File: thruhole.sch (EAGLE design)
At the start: 10 parts

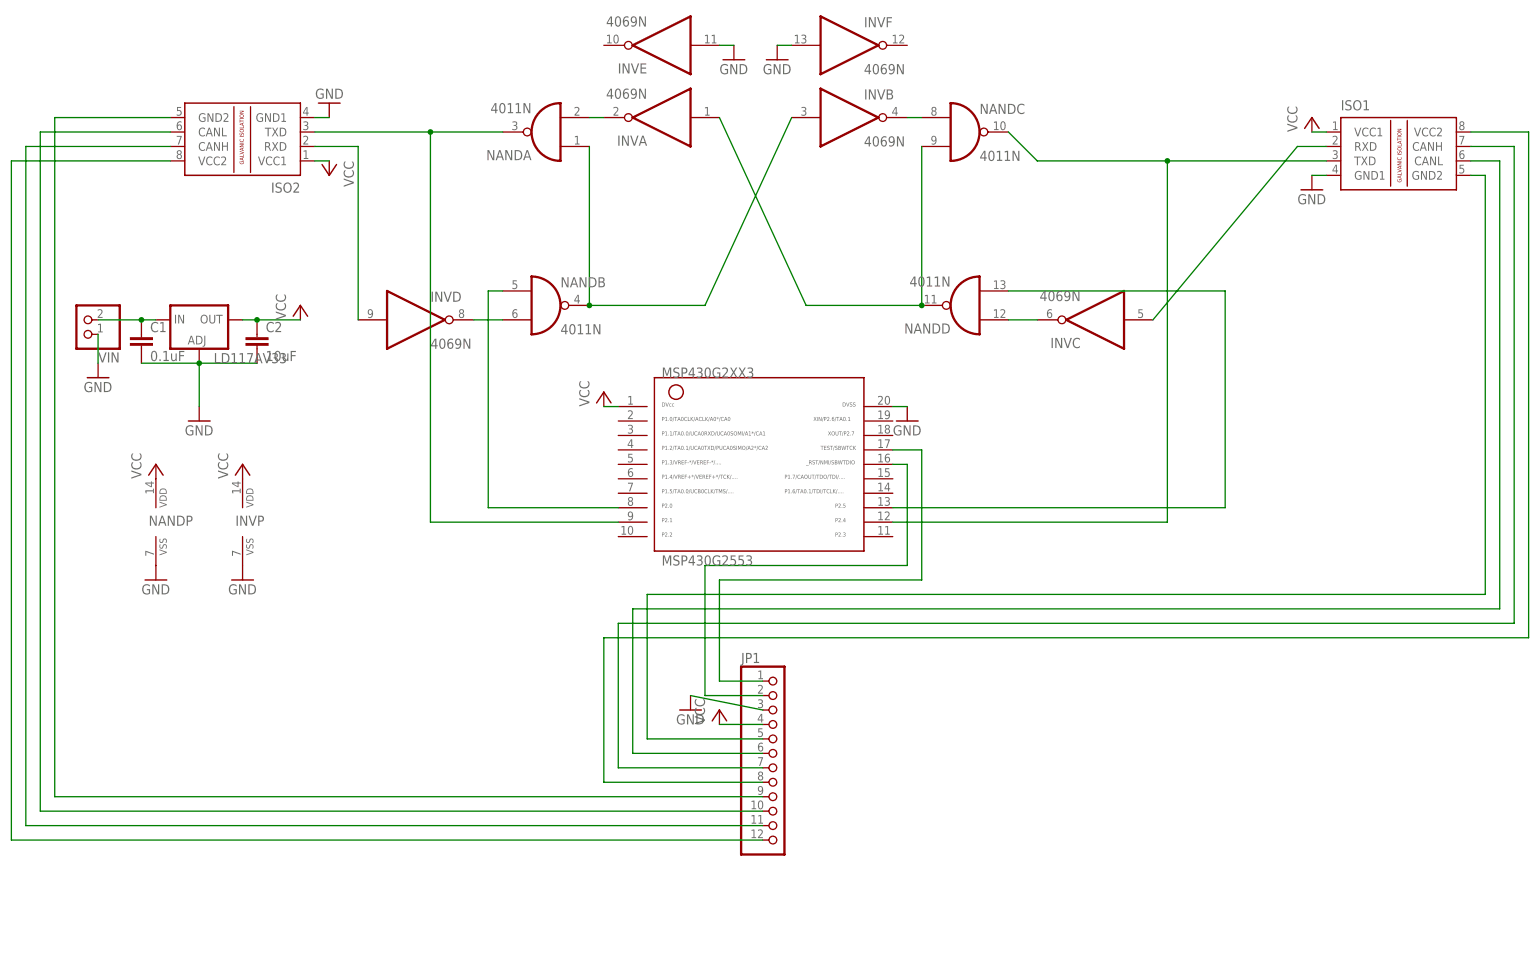
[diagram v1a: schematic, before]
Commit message: Separated thruhole 1x12 pin header into 3 1x4 pin headers for rules compliance
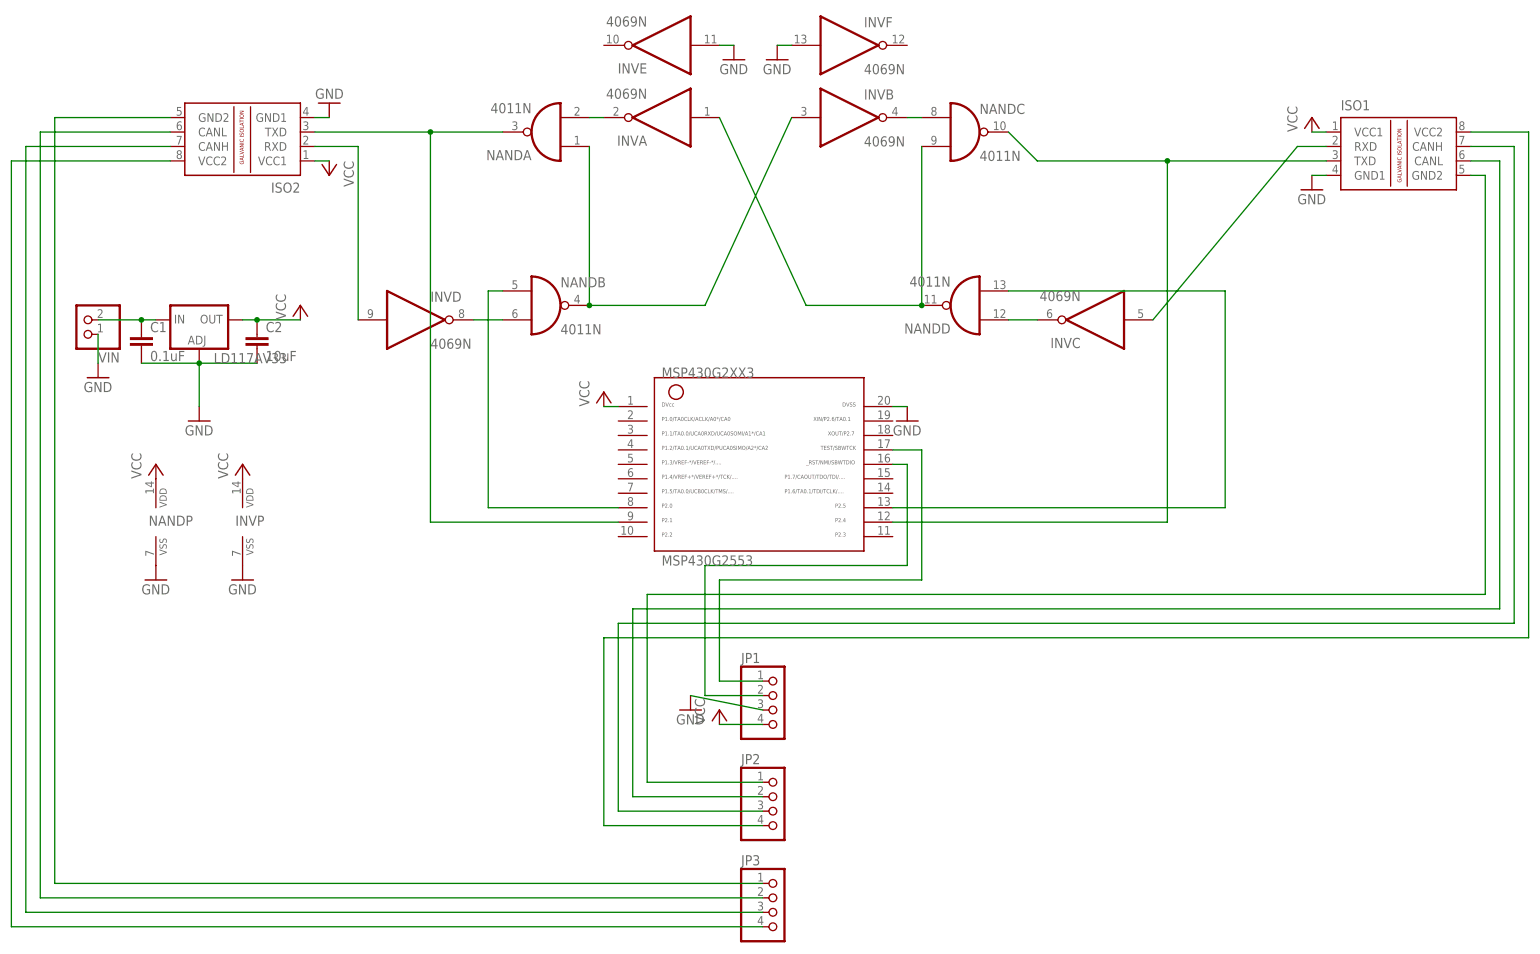
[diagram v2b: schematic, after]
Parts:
- added JP2, JP3: (no value), pinhead:PINHD-1X4
- JP1: device pinhead:PINHD-1X12 -> pinhead:PINHD-1X4
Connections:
- net N$10: now also JP3.3; no longer JP1.11
- net N$11: now also JP3.2; no longer JP1.10
- net N$12: now also JP3.1; no longer JP1.9
- net N$13: now also JP2.4; no longer JP1.8
- net N$14: now also JP2.3; no longer JP1.7
- net N$15: now also JP2.2; no longer JP1.6
- net N$16: now also JP2.1; no longer JP1.5
- net N$9: now also JP3.4; no longer JP1.12
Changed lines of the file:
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@@
 <setting verticaltext="up"/>
 </settings>
-<grid distance="0.1" unitdist="inch" unit="inch" style="lines" multiple="1" display="yes" altdistance="0.01" altunitdist="inch" altunit="inch"/>
+<grid distance="0.1" unitdist="inch" unit="inch" style="lines" multiple="1" display="no" altdistance="0.01" altunitdist="inch" altunit="inch"/>
 <layers>
 <layer number="1" name="Top" color="4" fill="1" visible="no" active="no"/>
@@
 <part name="GND11" library="supply1" deviceset="GND" device=""/>
 <part name="MSP430G2553" library="TI_MSP430_v16" deviceset="G2XX3---N20" device="" value=""/>
-<part name="JP1" library="pinhead" deviceset="PINHD-1X12" device=""/>
 <part name="GND9" library="supply1" deviceset="GND" device=""/>
 <part name="P+8" library="supply1" deviceset="VCC" device=""/>
+<part name="JP1" library="pinhead" deviceset="PINHD-1X4" device=""/>
+<part name="JP2" library="pinhead" deviceset="PINHD-1X4" device=""/>
+<part name="JP3" library="pinhead" deviceset="PINHD-1X4" device=""/>
 </parts>
 <sheets>
@@
 <instance part="GND11" gate="1" x="127" y="99.06"/>
 <instance part="MSP430G2553" gate="G$1" x="124.46" y="30.48"/>
-<instance part="JP1" gate="G$1" x="127" y="-22.86"/>
 <instance part="GND9" gate="1" x="111.76" y="-15.24"/>
 <instance part="P+8" gate="VCC" x="116.84" y="-15.24"/>
+<instance part="JP1" gate="A" x="127" y="-15.24"/>
+<instance part="JP2" gate="A" x="127" y="-33.02"/>
+<instance part="JP3" gate="A" x="127" y="-50.8"/>
 </instances>
 <busses>
@@
 </segment>
 <segment>
-<pinref part="JP1" gate="G$1" pin="4"/>
 <pinref part="P+8" gate="VCC" pin="VCC"/>
 <wire x1="124.46" y1="-17.78" x2="116.84" y2="-17.78" width="0.1524" layer="91"/>
+<pinref part="JP1" gate="A" pin="4"/>
 </segment>
 </net>
@@
 </segment>
 <segment>
-<pinref part="JP1" gate="G$1" pin="3"/>
 <pinref part="GND9" gate="1" pin="GND"/>
 <wire x1="124.46" y1="-15.24" x2="111.76" y2="-12.7" width="0.1524" layer="91"/>
+<pinref part="JP1" gate="A" pin="3"/>
 </segment>
 </net>
@@
 <wire x1="149.86" y1="10.16" x2="114.3" y2="10.16" width="0.1524" layer="91"/>
 <wire x1="114.3" y1="10.16" x2="114.3" y2="-12.7" width="0.1524" layer="91"/>
-<pinref part="JP1" gate="G$1" pin="2"/>
 <wire x1="114.3" y1="-12.7" x2="124.46" y2="-12.7" width="0.1524" layer="91"/>
+<pinref part="JP1" gate="A" pin="2"/>
 </segment>
 </net>
@@
 <wire x1="152.4" y1="7.62" x2="116.84" y2="7.62" width="0.1524" layer="91"/>
 <wire x1="116.84" y1="7.62" x2="116.84" y2="-10.16" width="0.1524" layer="91"/>
-<pinref part="JP1" gate="G$1" pin="1"/>
 <wire x1="116.84" y1="-10.16" x2="124.46" y2="-10.16" width="0.1524" layer="91"/>
+<pinref part="JP1" gate="A" pin="1"/>
 </segment>
 </net>
@@
 <wire x1="259.08" y1="86.36" x2="259.08" y2="-2.54" width="0.1524" layer="91"/>
 <wire x1="259.08" y1="-2.54" x2="96.52" y2="-2.54" width="0.1524" layer="91"/>
-<pinref part="JP1" gate="G$1" pin="8"/>
-<wire x1="96.52" y1="-2.54" x2="96.52" y2="-27.94" width="0.1524" layer="91"/>
-<wire x1="96.52" y1="-27.94" x2="124.46" y2="-27.94" width="0.1524" layer="91"/>
+<wire x1="96.52" y1="-2.54" x2="96.52" y2="-35.56" width="0.1524" layer="91"/>
+<wire x1="96.52" y1="-35.56" x2="124.46" y2="-35.56" width="0.1524" layer="91"/>
+<pinref part="JP2" gate="A" pin="4"/>
 </segment>
 </net>
@@
 <wire x1="256.54" y1="83.82" x2="256.54" y2="0" width="0.1524" layer="91"/>
 <wire x1="256.54" y1="0" x2="99.06" y2="0" width="0.1524" layer="91"/>
-<pinref part="JP1" gate="G$1" pin="7"/>
-<wire x1="99.06" y1="0" x2="99.06" y2="-25.4" width="0.1524" layer="91"/>
-<wire x1="99.06" y1="-25.4" x2="124.46" y2="-25.4" width="0.1524" layer="91"/>
+<wire x1="99.06" y1="0" x2="99.06" y2="-33.02" width="0.1524" layer="91"/>
+<wire x1="99.06" y1="-33.02" x2="124.46" y2="-33.02" width="0.1524" layer="91"/>
+<pinref part="JP2" gate="A" pin="3"/>
 </segment>
 </net>
@@
 <wire x1="254" y1="81.28" x2="254" y2="2.54" width="0.1524" layer="91"/>
 <wire x1="254" y1="2.54" x2="101.6" y2="2.54" width="0.1524" layer="91"/>
-<pinref part="JP1" gate="G$1" pin="6"/>
-<wire x1="101.6" y1="2.54" x2="101.6" y2="-22.86" width="0.1524" layer="91"/>
-<wire x1="101.6" y1="-22.86" x2="124.46" y2="-22.86" width="0.1524" layer="91"/>
+<wire x1="101.6" y1="2.54" x2="101.6" y2="-30.48" width="0.1524" layer="91"/>
+<wire x1="101.6" y1="-30.48" x2="124.46" y2="-30.48" width="0.1524" layer="91"/>
+<pinref part="JP2" gate="A" pin="2"/>
 </segment>
 </net>
@@
 <wire x1="251.46" y1="78.74" x2="251.46" y2="5.08" width="0.1524" layer="91"/>
 <wire x1="251.46" y1="5.08" x2="104.14" y2="5.08" width="0.1524" layer="91"/>
-<pinref part="JP1" gate="G$1" pin="5"/>
-<wire x1="104.14" y1="5.08" x2="104.14" y2="-20.32" width="0.1524" layer="91"/>
-<wire x1="104.14" y1="-20.32" x2="124.46" y2="-20.32" width="0.1524" layer="91"/>
+<wire x1="104.14" y1="5.08" x2="104.14" y2="-27.94" width="0.1524" layer="91"/>
+<wire x1="104.14" y1="-27.94" x2="124.46" y2="-27.94" width="0.1524" layer="91"/>
+<pinref part="JP2" gate="A" pin="1"/>
 </segment>
 </net>
@@
 <pinref part="ISO2" gate="G$1" pin="VCC2"/>
 <wire x1="20.32" y1="81.28" x2="-7.62" y2="81.28" width="0.1524" layer="91"/>
-<wire x1="-7.62" y1="81.28" x2="-7.62" y2="-38.1" width="0.1524" layer="91"/>
-<pinref part="JP1" gate="G$1" pin="12"/>
-<wire x1="-7.62" y1="-38.1" x2="124.46" y2="-38.1" width="0.1524" layer="91"/>
+<wire x1="-7.62" y1="81.28" x2="-7.62" y2="-53.34" width="0.1524" layer="91"/>
+<wire x1="-7.62" y1="-53.34" x2="124.46" y2="-53.34" width="0.1524" layer="91"/>
+<pinref part="JP3" gate="A" pin="4"/>
 </segment>
 </net>
@@
 <pinref part="ISO2" gate="G$1" pin="CANH"/>
 <wire x1="20.32" y1="83.82" x2="-5.08" y2="83.82" width="0.1524" layer="91"/>
-<wire x1="-5.08" y1="83.82" x2="-5.08" y2="-35.56" width="0.1524" layer="91"/>
-<pinref part="JP1" gate="G$1" pin="11"/>
-<wire x1="-5.08" y1="-35.56" x2="124.46" y2="-35.56" width="0.1524" layer="91"/>
+<wire x1="-5.08" y1="83.82" x2="-5.08" y2="-50.8" width="0.1524" layer="91"/>
+<wire x1="-5.08" y1="-50.8" x2="124.46" y2="-50.8" width="0.1524" layer="91"/>
+<pinref part="JP3" gate="A" pin="3"/>
 </segment>
 </net>
@@
 <pinref part="ISO2" gate="G$1" pin="CANL"/>
 <wire x1="20.32" y1="86.36" x2="-2.54" y2="86.36" width="0.1524" layer="91"/>
-<wire x1="-2.54" y1="86.36" x2="-2.54" y2="-33.02" width="0.1524" layer="91"/>
-<pinref part="JP1" gate="G$1" pin="10"/>
-<wire x1="-2.54" y1="-33.02" x2="124.46" y2="-33.02" width="0.1524" layer="91"/>
+<wire x1="-2.54" y1="86.36" x2="-2.54" y2="-48.26" width="0.1524" layer="91"/>
+<wire x1="-2.54" y1="-48.26" x2="124.46" y2="-48.26" width="0.1524" layer="91"/>
+<pinref part="JP3" gate="A" pin="2"/>
 </segment>
 </net>
@@
 <pinref part="ISO2" gate="G$1" pin="GND2"/>
 <wire x1="20.32" y1="88.9" x2="0" y2="88.9" width="0.1524" layer="91"/>
-<wire x1="0" y1="88.9" x2="0" y2="-30.48" width="0.1524" layer="91"/>
-<pinref part="JP1" gate="G$1" pin="9"/>
-<wire x1="0" y1="-30.48" x2="124.46" y2="-30.48" width="0.1524" layer="91"/>
-</segment>
-</net>
+<wire x1="0" y1="88.9" x2="0" y2="-45.72" width="0.1524" layer="91"/>
+<wire x1="0" y1="-45.72" x2="124.46" y2="-45.72" width="0.1524" layer="91"/>
+<pinref part="JP3" gate="A" pin="1"/>
+</segment>
+</net>
